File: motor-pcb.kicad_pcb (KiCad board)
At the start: 2 copper layers, 99 x 78 mm, 20 parts, among them J1 Power Input, J2 Motor, J3 Optocoupler, J5 Connection with second PCB, U1 LM7812_TO220, U2 INA219BxDCN, U3 LM7805_TO220, U4 TMP117xxDRV

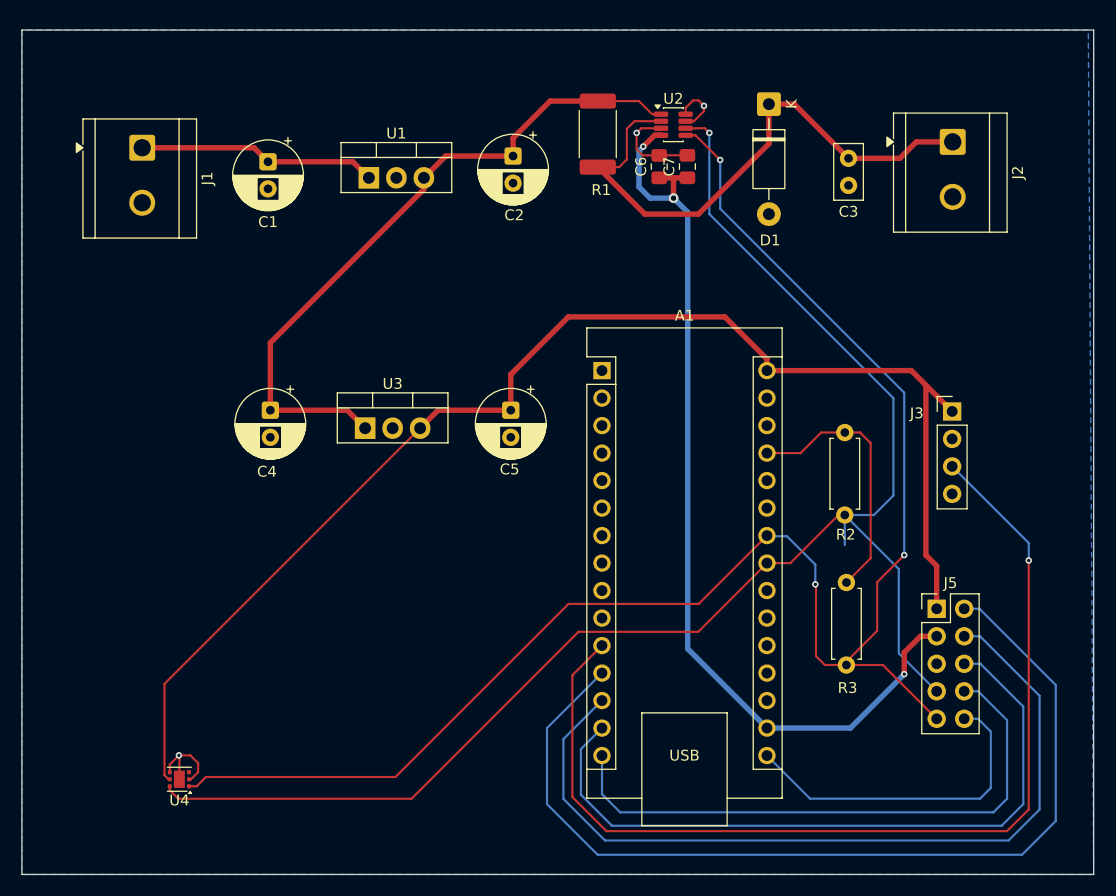
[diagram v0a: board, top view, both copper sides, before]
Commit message: Updated PCB layout: improved routing and component placement
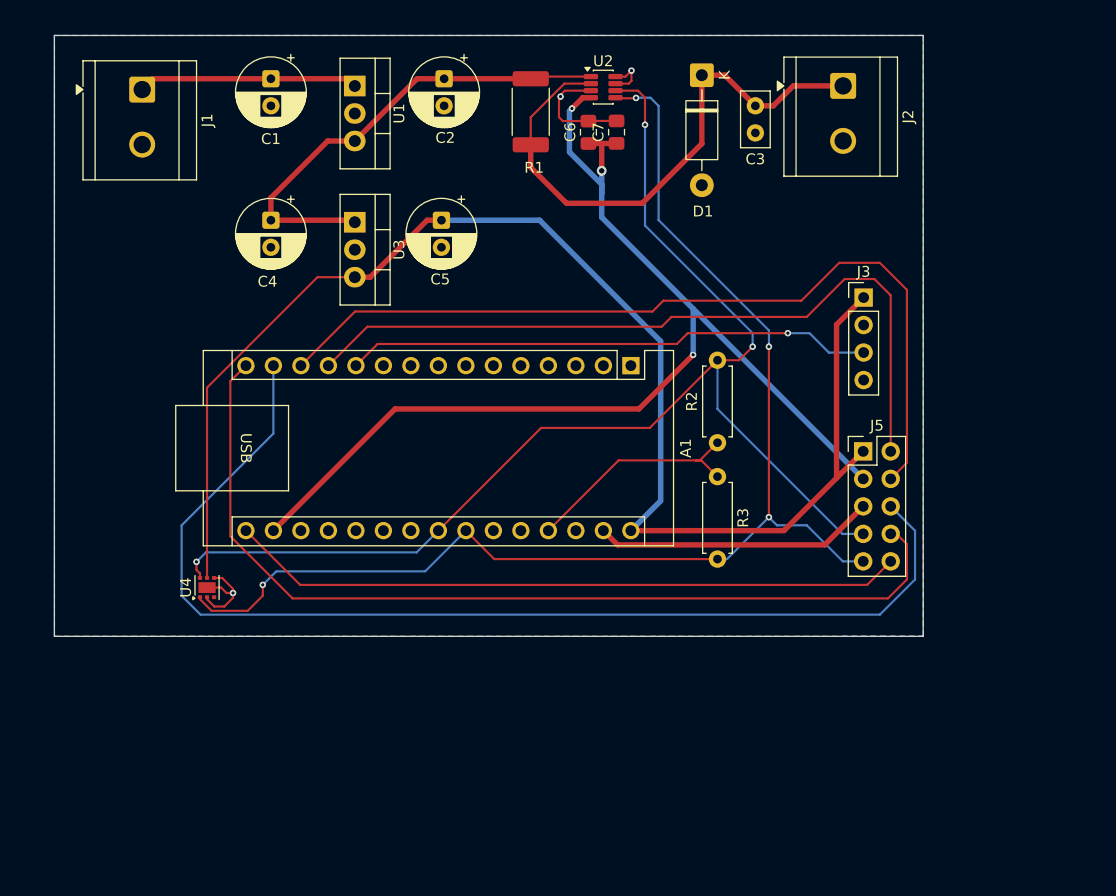
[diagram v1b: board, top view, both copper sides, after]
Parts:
- moved U3 19.1 mm to (104.8, 85.8), turned to -90 degrees
- moved C5 18.7 mm to (112.8, 85.6)
- moved U4 17.9 mm to (91.1, 119.5), turned to 90 degrees
- moved C4 17.6 mm to (97.0, 85.6)
- moved J5 16.0 mm to (151.7, 106.9)
- moved R3 15.4 mm to (138.2, 109.2)
- moved J3 13.3 mm to (151.8, 92.7)
- moved R2 11.8 mm to (138.2, 106.1), turned to 90 degrees
- moved J2 11.4 mm to (149.9, 73.2)
- moved C3 9.88 mm to (141.8, 75.0)
- moved C2 9.57 mm to (113.0, 72.5)
- moved U1 8.58 mm to (104.8, 73.2), turned to -90 degrees
- moved C1 7.67 mm to (97.0, 72.5)
- moved U2 7.35 mm to (127.7, 73.3)
- moved C6 7.27 mm to (126.3, 77.4)
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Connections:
- U4 pad 7: (no net) -> GND
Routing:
- net D8: track 94.0 -> 48.9 mm
- net D11: track 66.0 -> 102.3 mm
- net SCL: track 150.6 -> 116.5 mm, vias 3 -> 4
- net D12: track 54.5 -> 87.6 mm
- net D13: track 30.9 -> 62.5 mm
- net SDA: track 144.6 -> 114.1 mm, vias 1 -> 3
- net GND: track 23.6 -> 49.6 mm
- net +12V: track 63.1 -> 44.8 mm
- net D9: track 88.4 -> 70.3 mm
- net +3.3V: track 87.2 -> 104.7 mm
- net +5V: track 123.6 -> 131.3 mm
- net Net-(A1-+5V): track 24.6 -> 21.6 mm
- net D10: track 77.1 -> 79.0 mm
- net Net-(J1-Pin_1): track 22.1 -> 20.3 mm
- net Net-(D1-K): track 52.9 -> 52.2 mm
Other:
- board size 99 x 78 mm -> 80.2 x 55.5 mm

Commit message: Updated shunt resistor value, footprints, layout
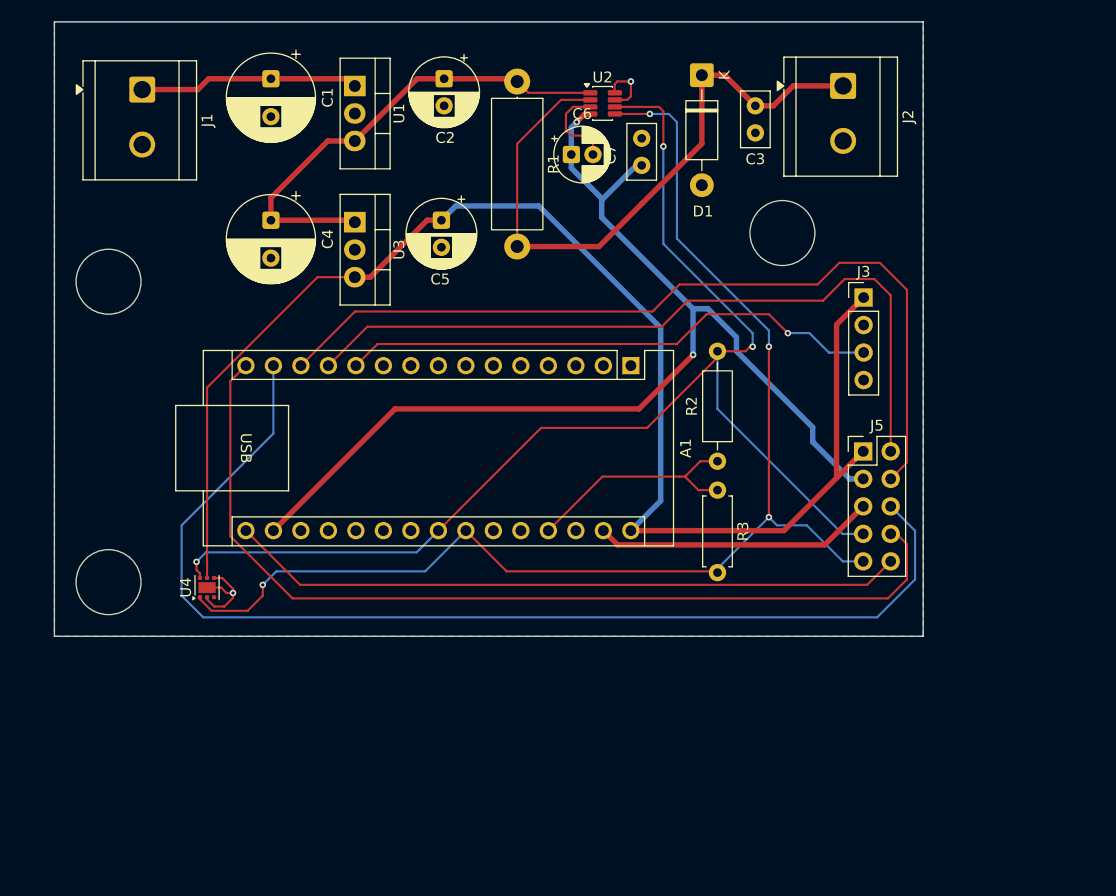
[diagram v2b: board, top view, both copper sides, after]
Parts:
- C1, C4: footprint Capacitor_THT:CP_Radial_D6.3mm_P2.50mm -> Capacitor_THT:CP_Radial_D8.0mm_P3.50mm
- C6: footprint Capacitor_SMD:C_0805_2012Metric_Pad1.18x1.45mm_HandSolder -> Capacitor_THT:CP_Radial_D5.0mm_P2.00mm
- C7: footprint Capacitor_SMD:C_0805_2012Metric_Pad1.18x1.45mm_HandSolder -> Capacitor_THT:C_Disc_D5.0mm_W2.5mm_P2.50mm
- R1: value 2mΩ -> 25mΩ; footprint Resistor_SMD:R_2512_6332Metric_Pad1.40x3.35mm_HandSolder -> Resistor_THT:R_Axial_DIN0414_L11.9mm_D4.5mm_P15.24mm_Horizontal
- R2: footprint Resistor_THT:R_Axial_DIN0207_L6.3mm_D2.5mm_P7.62mm_Horizontal -> Resistor_THT:R_Axial_DIN0207_L6.3mm_D2.5mm_P10.16mm_Horizontal
- moved C7 3.85 mm to (131.2, 80.5)
- moved R1 3.06 mm to (119.8, 72.8)
- moved C6 2.59 mm to (124.8, 79.5), turned to 0 degrees
- moved R2 1.71 mm to (138.2, 107.8)
- moved U2 1.50 mm to (127.6, 74.8)
- moved R3 1.25 mm to (138.2, 110.5)
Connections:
- U4 pad 7: GND -> (no net)
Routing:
- net Net-(D1-K): track 52.2 -> 60.2 mm
- net +5V: track 131.3 -> 133.2 mm
- net +3.3V: track 104.7 -> 103.1 mm, vias 3 -> 2
- net D8: track 48.9 -> 50.3 mm
- net GND: track 49.6 -> 48.3 mm, vias 3 -> 2
- net SDA: track 114.1 -> 114.9 mm
- net SCL: track 116.5 -> 117.3 mm
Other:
- board size 80.2 x 55.5 mm -> 80.2 x 56.8 mm
